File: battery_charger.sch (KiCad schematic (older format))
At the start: 23 parts

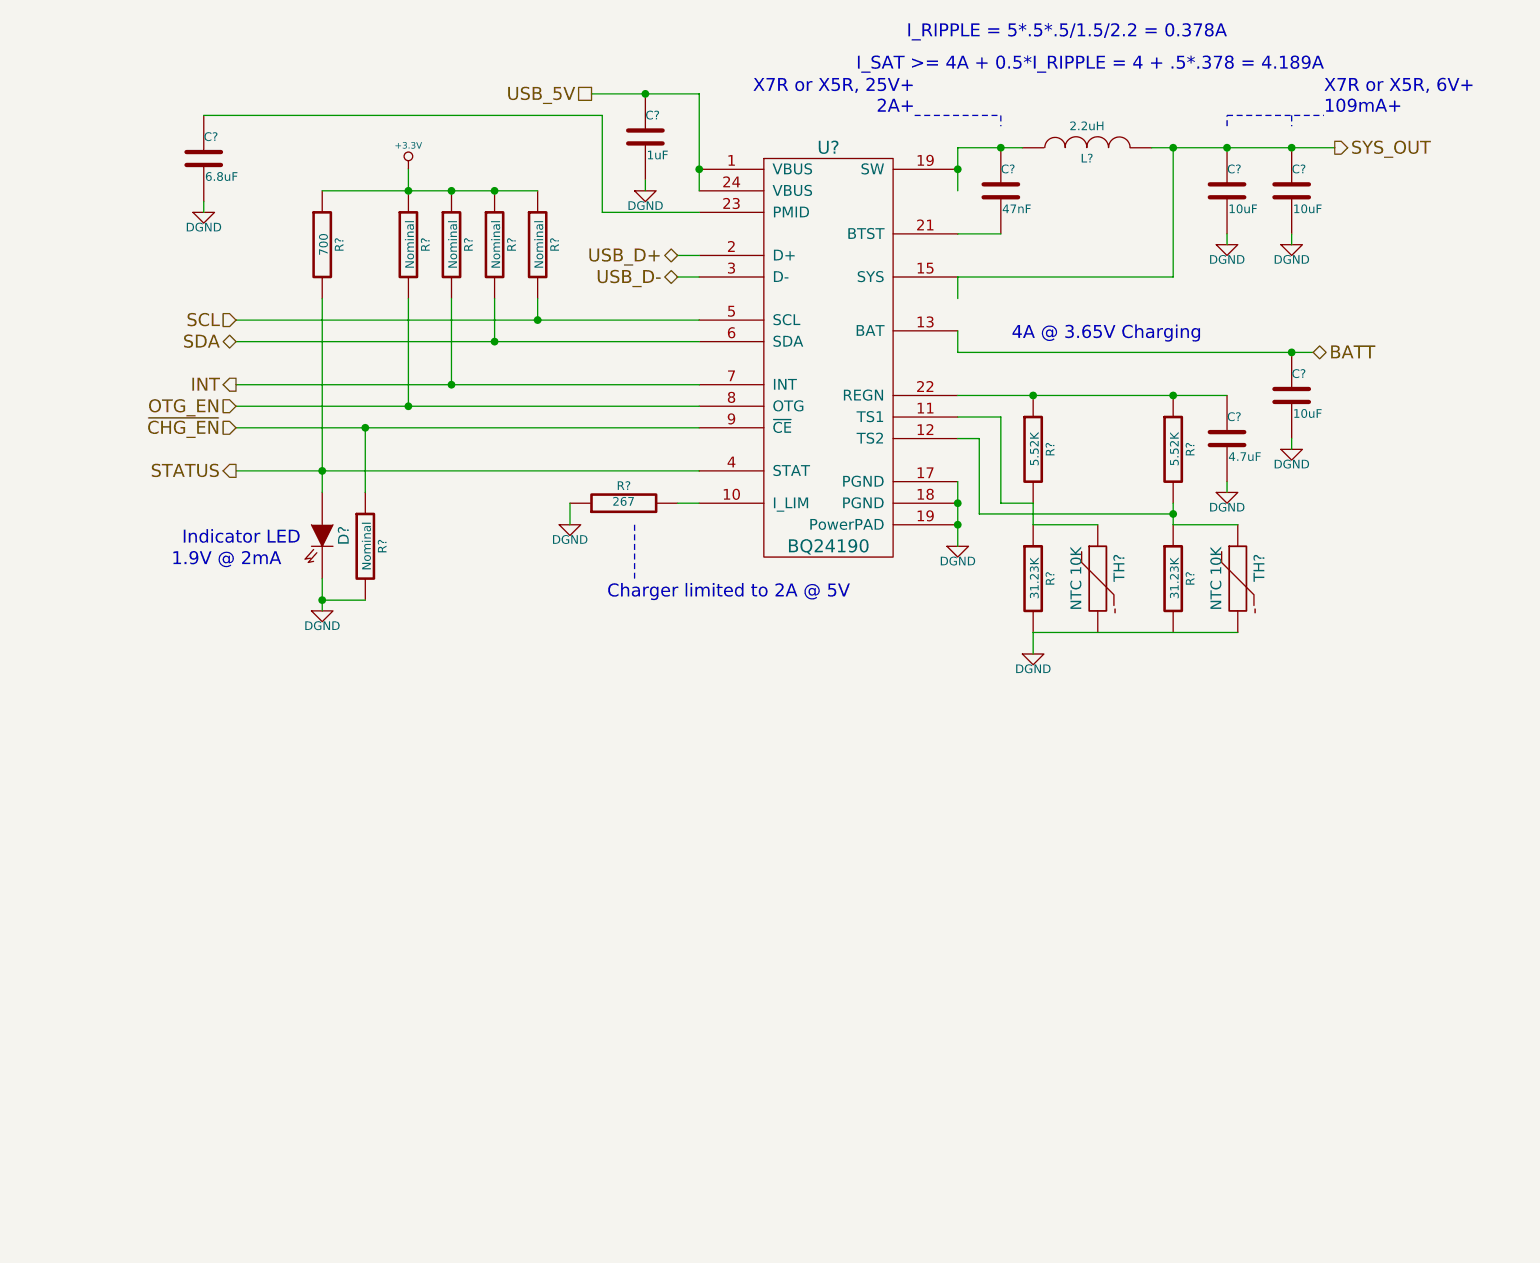
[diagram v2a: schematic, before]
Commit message: various fixes due to issues found in ERC
learned how to use invisible pins
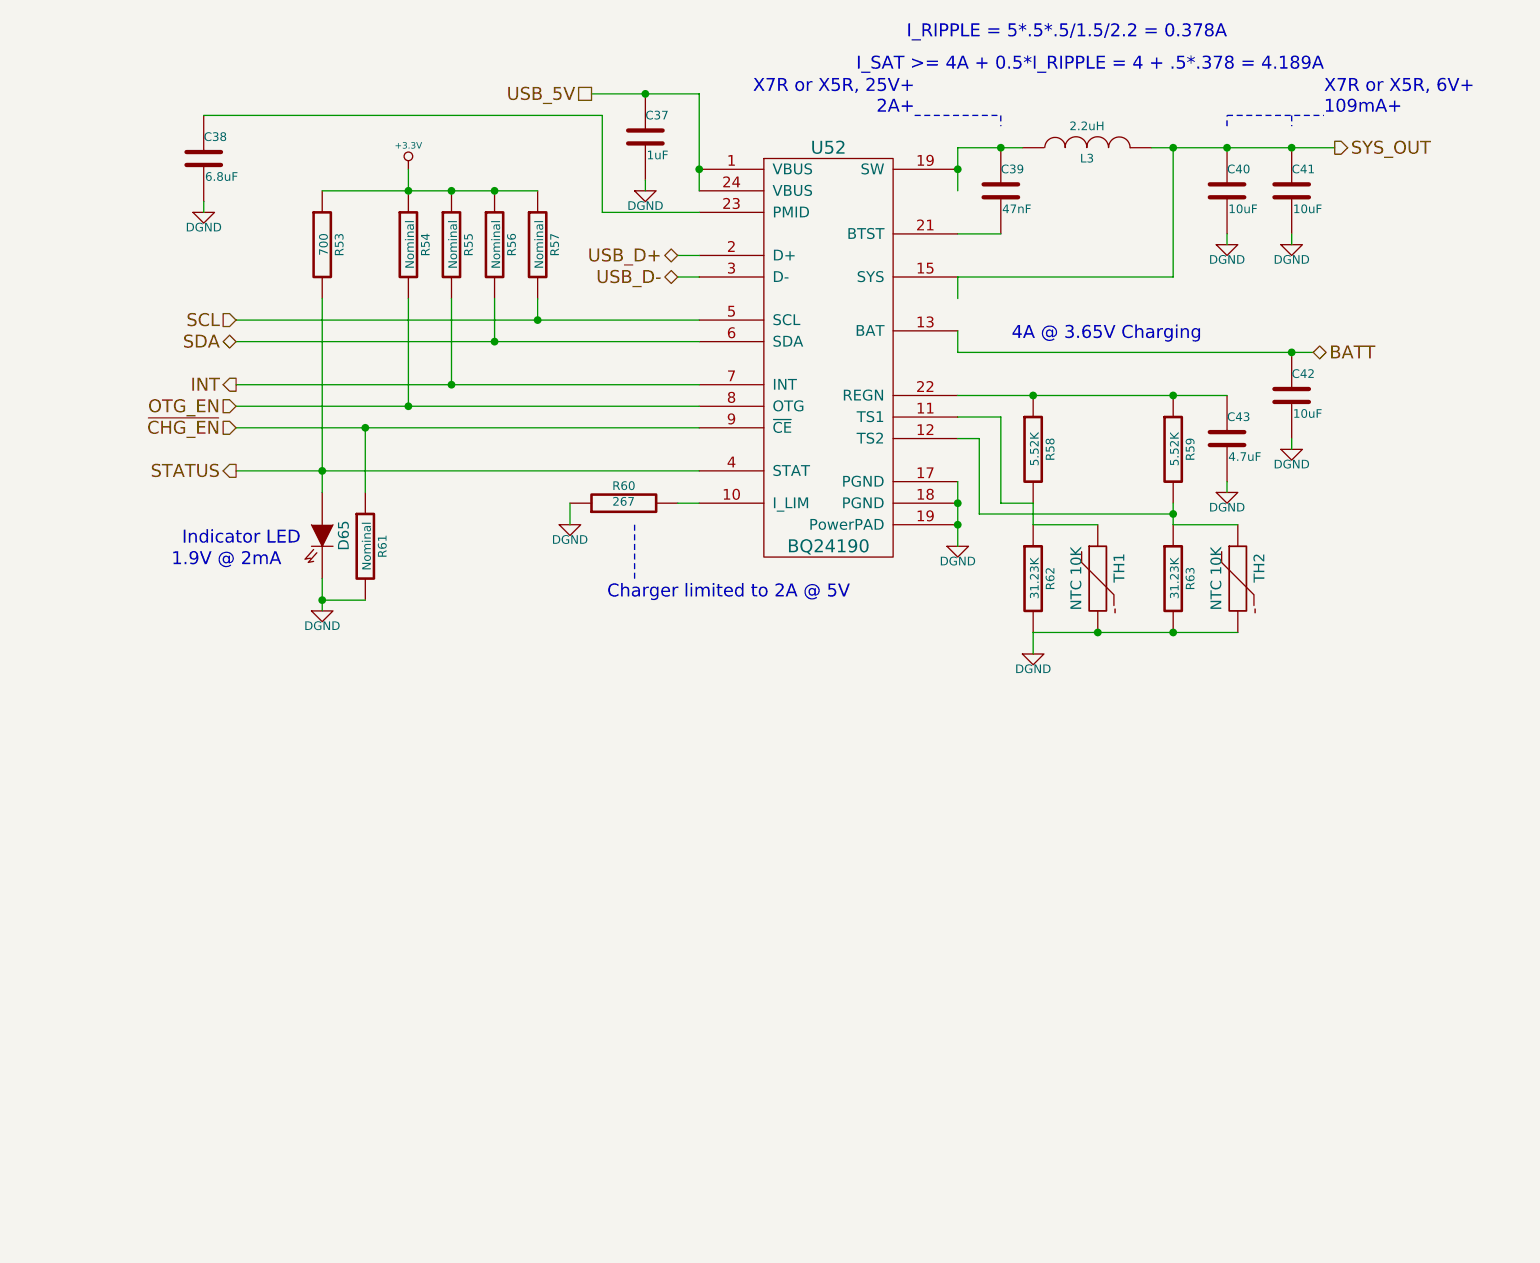
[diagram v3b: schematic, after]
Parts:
- gave numbers to parts that had none: 23
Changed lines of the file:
@@
 Sheet 18 18
 Title ""
-Date "18 dec 2013"
+Date "20 dec 2013"
 Rev ""
 Comp ""
@@
 USB_D-
 $Comp
-L DGND #PWR?
+L DGND #PWR0120
 U 1 1 5292B82E
 P 3600 3400
-F 0 "#PWR?" H 3600 3400 40  0001 C CNN
+F 0 "#PWR0120" H 3600 3400 40  0001 C CNN
 F 1 "DGND" H 3600 3330 40  0000 C CNN
 F 2 "" H 3600 3400 60  0000 C CNN
@@
 $EndComp
 $Comp
-L R R?
+L R R55
 U 1 1 5292B87D
 P 3050 2100
-F 0 "R?" V 3130 2100 40  0000 C CNN
+F 0 "R55" V 3130 2100 40  0000 C CNN
 F 1 "Nominal" V 3057 2101 40  0000 C CNN
 F 2 "~" V 2980 2100 30  0000 C CNN
@@
 $EndComp
 $Comp
-L R R?
+L R R56
 U 1 1 5292B883
 P 3250 2100
-F 0 "R?" V 3330 2100 40  0000 C CNN
+F 0 "R56" V 3330 2100 40  0000 C CNN
 F 1 "Nominal" V 3257 2101 40  0000 C CNN
 F 2 "~" V 3180 2100 30  0000 C CNN
@@
 $EndComp
 $Comp
-L R R?
+L R R57
 U 1 1 5292B889
 P 3450 2100
-F 0 "R?" V 3530 2100 40  0000 C CNN
+F 0 "R57" V 3530 2100 40  0000 C CNN
 F 1 "Nominal" V 3457 2101 40  0000 C CNN
 F 2 "~" V 3380 2100 30  0000 C CNN
@@
 $EndComp
 $Comp
-L R R?
+L R R58
 U 1 1 5292B88F
 P 5750 3050
-F 0 "R?" V 5830 3050 40  0000 C CNN
+F 0 "R58" V 5830 3050 40  0000 C CNN
 F 1 "5.52K" V 5757 3051 40  0000 C CNN
 F 2 "~" V 5680 3050 30  0000 C CNN
@@
 $EndComp
 $Comp
-L R R?
+L R R62
 U 1 1 5292B895
 P 5750 3650
-F 0 "R?" V 5830 3650 40  0000 C CNN
+F 0 "R62" V 5830 3650 40  0000 C CNN
 F 1 "31.23K" V 5757 3651 40  0000 C CNN
 F 2 "~" V 5680 3650 30  0000 C CNN
@@
 $EndComp
 $Comp
-L R R?
+L R R59
 U 1 1 5292B89B
 P 6400 3050
-F 0 "R?" V 6480 3050 40  0000 C CNN
+F 0 "R59" V 6480 3050 40  0000 C CNN
 F 1 "5.52K" V 6407 3051 40  0000 C CNN
 F 2 "~" V 6330 3050 30  0000 C CNN
@@
 $EndComp
 $Comp
-L R R?
+L R R63
 U 1 1 5292B8A1
 P 6400 3650
-F 0 "R?" V 6480 3650 40  0000 C CNN
+F 0 "R63" V 6480 3650 40  0000 C CNN
 F 1 "31.23K" V 6407 3651 40  0000 C CNN
 F 2 "~" V 6330 3650 30  0000 C CNN
@@
 $EndComp
 $Comp
-L R R?
+L R R60
 U 1 1 5292B8A7
 P 3850 3300
-F 0 "R?" V 3930 3300 40  0000 C CNN
+F 0 "R60" V 3930 3300 40  0000 C CNN
 F 1 "267" V 3857 3301 40  0000 C CNN
 F 2 "~" V 3780 3300 30  0000 C CNN
@@
 STATUS
 $Comp
-L THERMISTOR TH?
+L THERMISTOR TH1
 U 1 1 52A9865D
 P 6050 3650
-F 0 "TH?" V 6150 3700 50  0000 C CNN
+F 0 "TH1" V 6150 3700 50  0000 C CNN
 F 1 "NTC 10K" V 5950 3650 50  0000 C CNN
 F 2 "~" H 6050 3650 60  0000 C CNN
@@
 $EndComp
 $Comp
-L THERMISTOR TH?
+L THERMISTOR TH2
 U 1 1 52A9866A
 P 6700 3650
-F 0 "TH?" V 6800 3700 50  0000 C CNN
+F 0 "TH2" V 6800 3700 50  0000 C CNN
 F 1 "NTC 10K" V 6600 3650 50  0000 C CNN
 F 2 "~" H 6700 3650 60  0000 C CNN
@@
 $EndComp
 $Comp
-L BQ24190 U?
+L BQ24190 U52
 U 1 1 52A98672
 P 4800 1650
-F 0 "U?" H 4800 1650 60  0000 C CNN
+F 0 "U52" H 4800 1650 60  0000 C CNN
 F 1 "BQ24190" H 4800 -200 60  0000 C CNN
 F 2 "~" H 4800 1650 60  0000 C CNN
@@
 $EndComp
 $Comp
-L DGND #PWR?
+L DGND #PWR0121
 U 1 1 52A986BA
 P 5400 3500
-F 0 "#PWR?" H 5400 3500 40  0001 C CNN
+F 0 "#PWR0121" H 5400 3500 40  0001 C CNN
 F 1 "DGND" H 5400 3430 40  0000 C CNN
 F 2 "" H 5400 3500 60  0000 C CNN
@@
 	5750 3900 6700 3900
 $Comp
-L DGND #PWR?
+L DGND #PWR0122
 U 1 1 52A98A95
 P 5750 4000
-F 0 "#PWR?" H 5750 4000 40  0001 C CNN
+F 0 "#PWR0122" H 5750 4000 40  0001 C CNN
 F 1 "DGND" H 5750 3930 40  0000 C CNN
 F 2 "" H 5750 4000 60  0000 C CNN
@@
 	4200 1400 4200 1850
 $Comp
-L C C?
+L C C37
 U 1 1 52AAD29A
 P 3950 1600
-F 0 "C?" H 3950 1700 40  0000 L CNN
+F 0 "C37" H 3950 1700 40  0000 L CNN
 F 1 "1uF" H 3956 1515 40  0000 L CNN
 F 2 "~" H 3988 1450 30  0000 C CNN
@@
 Connection ~ 3950 1400
 $Comp
-L DGND #PWR?
+L DGND #PWR0123
 U 1 1 52AAD37B
 P 3950 1850
-F 0 "#PWR?" H 3950 1850 40  0001 C CNN
+F 0 "#PWR0123" H 3950 1850 40  0001 C CNN
 F 1 "DGND" H 3950 1780 40  0000 C CNN
 F 2 "" H 3950 1850 60  0000 C CNN
@@
 	3750 1500 1900 1500
 $Comp
-L +3.3V #PWR?
+L +3.3V #PWR0124
 U 1 1 52AAD3EE
 P 2850 1750
-F 0 "#PWR?" H 2850 1710 30  0001 C CNN
+F 0 "#PWR0124" H 2850 1710 30  0001 C CNN
 F 1 "+3.3V" H 2850 1860 30  0000 C CNN
 F 2 "" H 2850 1750 60  0000 C CNN
@@
 Connection ~ 3250 1850
 $Comp
-L C C?
+L C C38
 U 1 1 52AAD4A2
 P 1900 1700
-F 0 "C?" H 1900 1800 40  0000 L CNN
+F 0 "C38" H 1900 1800 40  0000 L CNN
 F 1 "6.8uF" H 1906 1615 40  0000 L CNN
 F 2 "~" H 1938 1550 30  0000 C CNN
@@
 $EndComp
 $Comp
-L DGND #PWR?
+L DGND #PWR0125
 U 1 1 52AAD4B3
 P 1900 1950
-F 0 "#PWR?" H 1900 1950 40  0001 C CNN
+F 0 "#PWR0125" H 1900 1950 40  0001 C CNN
 F 1 "DGND" H 1900 1880 40  0000 C CNN
 F 2 "" H 1900 1950 60  0000 C CNN
@@
 	2050 3150 4200 3150
 $Comp
-L C C?
+L C C42
 U 1 1 52AB375A
 P 6950 2800
-F 0 "C?" H 6950 2900 40  0000 L CNN
+F 0 "C42" H 6950 2900 40  0000 L CNN
 F 1 "10uF" H 6956 2715 40  0000 L CNN
 F 2 "~" H 6988 2650 30  0000 C CNN
@@
 $EndComp
 $Comp
-L DGND #PWR?
+L DGND #PWR0126
 U 1 1 52AB3760
 P 6950 3050
-F 0 "#PWR?" H 6950 3050 40  0001 C CNN
+F 0 "#PWR0126" H 6950 3050 40  0001 C CNN
 F 1 "DGND" H 6950 2980 40  0000 C CNN
 F 2 "" H 6950 3050 60  0000 C CNN
@@
 Connection ~ 6950 2600
 $Comp
-L C C?
+L C C39
 U 1 1 52AB388A
 P 5600 1850
-F 0 "C?" H 5600 1950 40  0000 L CNN
+F 0 "C39" H 5600 1950 40  0000 L CNN
 F 1 "47nF" H 5606 1765 40  0000 L CNN
 F 2 "~" H 5638 1700 30  0000 C CNN
@@
 Connection ~ 5600 1650
 $Comp
-L INDUCTOR L?
+L INDUCTOR L3
 U 1 1 52AB3CD7
 P 6000 1650
-F 0 "L?" V 5950 1650 40  0000 C CNN
+F 0 "L3" V 5950 1650 40  0000 C CNN
 F 1 "2.2uH" V 6100 1650 40  0000 C CNN
 F 2 "~" H 6000 1650 60  0000 C CNN
@@
 Connection ~ 6400 2800
 $Comp
-L C C?
+L C C43
 U 1 1 52AB3E00
 P 6650 3000
-F 0 "C?" H 6650 3100 40  0000 L CNN
+F 0 "C43" H 6650 3100 40  0000 L CNN
 F 1 "4.7uF" H 6656 2915 40  0000 L CNN
 F 2 "~" H 6688 2850 30  0000 C CNN
@@
 $EndComp
 $Comp
-L DGND #PWR?
+L DGND #PWR0127
 U 1 1 52AB3E06
 P 6650 3250
-F 0 "#PWR?" H 6650 3250 40  0001 C CNN
+F 0 "#PWR0127" H 6650 3250 40  0001 C CNN
 F 1 "DGND" H 6650 3180 40  0000 C CNN
 F 2 "" H 6650 3250 60  0000 C CNN
@@
 Connection ~ 6400 1650
 $Comp
-L C C?
+L C C40
 U 1 1 52AB3EAE
 P 6650 1850
-F 0 "C?" H 6650 1950 40  0000 L CNN
+F 0 "C40" H 6650 1950 40  0000 L CNN
 F 1 "10uF" H 6656 1765 40  0000 L CNN
 F 2 "~" H 6688 1700 30  0000 C CNN
@@
 $EndComp
 $Comp
-L DGND #PWR?
+L DGND #PWR0128
 U 1 1 52AB3EB4
 P 6650 2100
-F 0 "#PWR?" H 6650 2100 40  0001 C CNN
+F 0 "#PWR0128" H 6650 2100 40  0001 C CNN
 F 1 "DGND" H 6650 2030 40  0000 C CNN
 F 2 "" H 6650 2100 60  0000 C CNN
@@
 	6650 2050 6650 2100
 $Comp
-L C C?
+L C C41
 U 1 1 52AB3EBB
 P 6950 1850
-F 0 "C?" H 6950 1950 40  0000 L CNN
+F 0 "C41" H 6950 1950 40  0000 L CNN
 F 1 "10uF" H 6956 1765 40  0000 L CNN
 F 2 "~" H 6988 1700 30  0000 C CNN
@@
 $EndComp
 $Comp
-L DGND #PWR?
+L DGND #PWR0129
 U 1 1 52AB3EC1
 P 6950 2100
-F 0 "#PWR?" H 6950 2100 40  0001 C CNN
+F 0 "#PWR0129" H 6950 2100 40  0001 C CNN
 F 1 "DGND" H 6950 2030 40  0000 C CNN
 F 2 "" H 6950 2100 60  0000 C CNN
@@
 Indicator LED
 $Comp
-L LED_GENERIC_SMD D?
+L LED_GENERIC_SMD D65
 U 1 1 52B37BFF
 P 2450 3450
-F 0 "D?" H 2450 3550 50  0000 C CNN
+F 0 "D65" H 2450 3550 50  0000 C CNN
 F 1 "LED_GENERIC_SMD" H 2450 3300 50  0001 C CNN
 F 2 "~" H 2450 3450 60  0000 C CNN
@@
 1.9V @ 2mA
 $Comp
-L DGND #PWR?
+L DGND #PWR0130
 U 1 1 52B37C0F
 P 2450 3800
-F 0 "#PWR?" H 2450 3800 40  0001 C CNN
+F 0 "#PWR0130" H 2450 3800 40  0001 C CNN
 F 1 "DGND" H 2450 3730 40  0000 C CNN
 F 2 "" H 2450 3800 60  0000 C CNN
@@
 Connection ~ 2850 1850
 $Comp
-L R R?
+L R R54
 U 1 1 52B3B9CF
 P 2850 2100
-F 0 "R?" V 2930 2100 40  0000 C CNN
+F 0 "R54" V 2930 2100 40  0000 C CNN
 F 1 "Nominal" V 2857 2101 40  0000 C CNN
 F 2 "~" V 2780 2100 30  0000 C CNN
@@
 Connection ~ 2850 2850
 $Comp
-L R R?
+L R R53
 U 1 1 52B3BA8E
 P 2450 2100
-F 0 "R?" V 2530 2100 40  0000 C CNN
+F 0 "R53" V 2530 2100 40  0000 C CNN
 F 1 "700" V 2457 2101 40  0000 C CNN
 F 2 "~" V 2380 2100 30  0000 C CNN
@@
 Connection ~ 2650 2950
 $Comp
-L R R?
+L R R61
 U 1 1 52B3BBFD
 P 2650 3500
-F 0 "R?" V 2730 3500 40  0000 C CNN
+F 0 "R61" V 2730 3500 40  0000 C CNN
 F 1 "Nominal" V 2657 3501 40  0000 C CNN
 F 2 "~" V 2580 3500 30  0000 C CNN
@@
 	2450 3750 2650 3750
 Connection ~ 2450 3750
+Connection ~ 6050 3900
+Connection ~ 6400 3900
 $EndSCHEMATC

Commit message: started figuring out how to get pcb going
also need to figure out how to make some footprints, although there is a
nice library of footprints avalible already
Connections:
- wire segments 54 -> 53
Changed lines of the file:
@@
 Sheet 18 18
 Title ""
-Date "20 dec 2013"
+Date "21 dec 2013"
 Rev ""
 Comp ""
@@
 USB_D-
 $Comp
-L DGND #PWR0120
+L DGND #PWR0124
 U 1 1 5292B82E
 P 3600 3400
-F 0 "#PWR0120" H 3600 3400 40  0001 C CNN
+F 0 "#PWR0124" H 3600 3400 40  0001 C CNN
 F 1 "DGND" H 3600 3330 40  0000 C CNN
 F 2 "" H 3600 3400 60  0000 C CNN
@@
 $EndComp
 $Comp
-L DGND #PWR0121
+L DGND #PWR0125
 U 1 1 52A986BA
 P 5400 3500
-F 0 "#PWR0121" H 5400 3500 40  0001 C CNN
+F 0 "#PWR0125" H 5400 3500 40  0001 C CNN
 F 1 "DGND" H 5400 3430 40  0000 C CNN
 F 2 "" H 5400 3500 60  0000 C CNN
@@
 	5750 3900 6700 3900
 $Comp
-L DGND #PWR0122
+L DGND #PWR0126
 U 1 1 52A98A95
 P 5750 4000
-F 0 "#PWR0122" H 5750 4000 40  0001 C CNN
+F 0 "#PWR0126" H 5750 4000 40  0001 C CNN
 F 1 "DGND" H 5750 3930 40  0000 C CNN
 F 2 "" H 5750 4000 60  0000 C CNN
@@
 Connection ~ 3950 1400
 $Comp
-L DGND #PWR0123
+L DGND #PWR0127
 U 1 1 52AAD37B
 P 3950 1850
-F 0 "#PWR0123" H 3950 1850 40  0001 C CNN
+F 0 "#PWR0127" H 3950 1850 40  0001 C CNN
 F 1 "DGND" H 3950 1780 40  0000 C CNN
 F 2 "" H 3950 1850 60  0000 C CNN
@@
 	3750 1500 1900 1500
 $Comp
-L +3.3V #PWR0124
+L +3.3V #PWR0128
 U 1 1 52AAD3EE
 P 2850 1750
-F 0 "#PWR0124" H 2850 1710 30  0001 C CNN
+F 0 "#PWR0128" H 2850 1710 30  0001 C CNN
 F 1 "+3.3V" H 2850 1860 30  0000 C CNN
 F 2 "" H 2850 1750 60  0000 C CNN
@@
 $EndComp
 $Comp
-L DGND #PWR0125
+L DGND #PWR0129
 U 1 1 52AAD4B3
 P 1900 1950
-F 0 "#PWR0125" H 1900 1950 40  0001 C CNN
+F 0 "#PWR0129" H 1900 1950 40  0001 C CNN
 F 1 "DGND" H 1900 1880 40  0000 C CNN
 F 2 "" H 1900 1950 60  0000 C CNN
@@
 $EndComp
 $Comp
-L DGND #PWR0126
+L DGND #PWR0130
 U 1 1 52AB3760
 P 6950 3050
-F 0 "#PWR0126" H 6950 3050 40  0001 C CNN
+F 0 "#PWR0130" H 6950 3050 40  0001 C CNN
 F 1 "DGND" H 6950 2980 40  0000 C CNN
 F 2 "" H 6950 3050 60  0000 C CNN
@@
 Wire Wire Line
 	6950 3000 6950 3050
-Wire Wire Line
-	5400 2500 5400 2600
 Wire Wire Line
 	5400 2600 7050 2600
@@
 	5400 2050 5600 2050
 Wire Wire Line
-	5400 1650 5400 1850
-Wire Wire Line
 	5400 1650 5700 1650
-Connection ~ 5400 1750
 Connection ~ 5600 1650
 $Comp
@@
 $EndComp
 Wire Wire Line
-	5400 2350 5400 2250
-Wire Wire Line
 	6300 1650 7150 1650
 Wire Wire Line
@@
 $EndComp
 $Comp
-L DGND #PWR0127
+L DGND #PWR0131
 U 1 1 52AB3E06
 P 6650 3250
-F 0 "#PWR0127" H 6650 3250 40  0001 C CNN
+F 0 "#PWR0131" H 6650 3250 40  0001 C CNN
 F 1 "DGND" H 6650 3180 40  0000 C CNN
 F 2 "" H 6650 3250 60  0000 C CNN
@@
 $EndComp
 $Comp
-L DGND #PWR0128
+L DGND #PWR0132
 U 1 1 52AB3EB4
 P 6650 2100
-F 0 "#PWR0128" H 6650 2100 40  0001 C CNN
+F 0 "#PWR0132" H 6650 2100 40  0001 C CNN
 F 1 "DGND" H 6650 2030 40  0000 C CNN
 F 2 "" H 6650 2100 60  0000 C CNN
@@
 $EndComp
 $Comp
-L DGND #PWR0129
+L DGND #PWR0133
 U 1 1 52AB3EC1
 P 6950 2100
-F 0 "#PWR0129" H 6950 2100 40  0001 C CNN
+F 0 "#PWR0133" H 6950 2100 40  0001 C CNN
 F 1 "DGND" H 6950 2030 40  0000 C CNN
 F 2 "" H 6950 2100 60  0000 C CNN
@@
 1.9V @ 2mA
 $Comp
-L DGND #PWR0130
+L DGND #PWR0134
 U 1 1 52B37C0F
 P 2450 3800
-F 0 "#PWR0130" H 2450 3800 40  0001 C CNN
+F 0 "#PWR0134" H 2450 3800 40  0001 C CNN
 F 1 "DGND" H 2450 3730 40  0000 C CNN
 F 2 "" H 2450 3800 60  0000 C CNN
@@
 Connection ~ 6050 3900
 Connection ~ 6400 3900
+Wire Wire Line
+	5400 1650 5400 1750
+Wire Wire Line
+	5400 2500 5400 2600
 $EndSCHEMATC
